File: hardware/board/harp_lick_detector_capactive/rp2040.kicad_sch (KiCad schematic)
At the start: 40 parts, among them J1 USB_C_Receptacle_USB2.0, J3 Conn_01x03_Male, J4 AudioJack3, U1 RP2040, U2 W25Q128JVS, U3 ADUM4160, U4 TPD2EUSB30, X1 ECS-TXO-2016

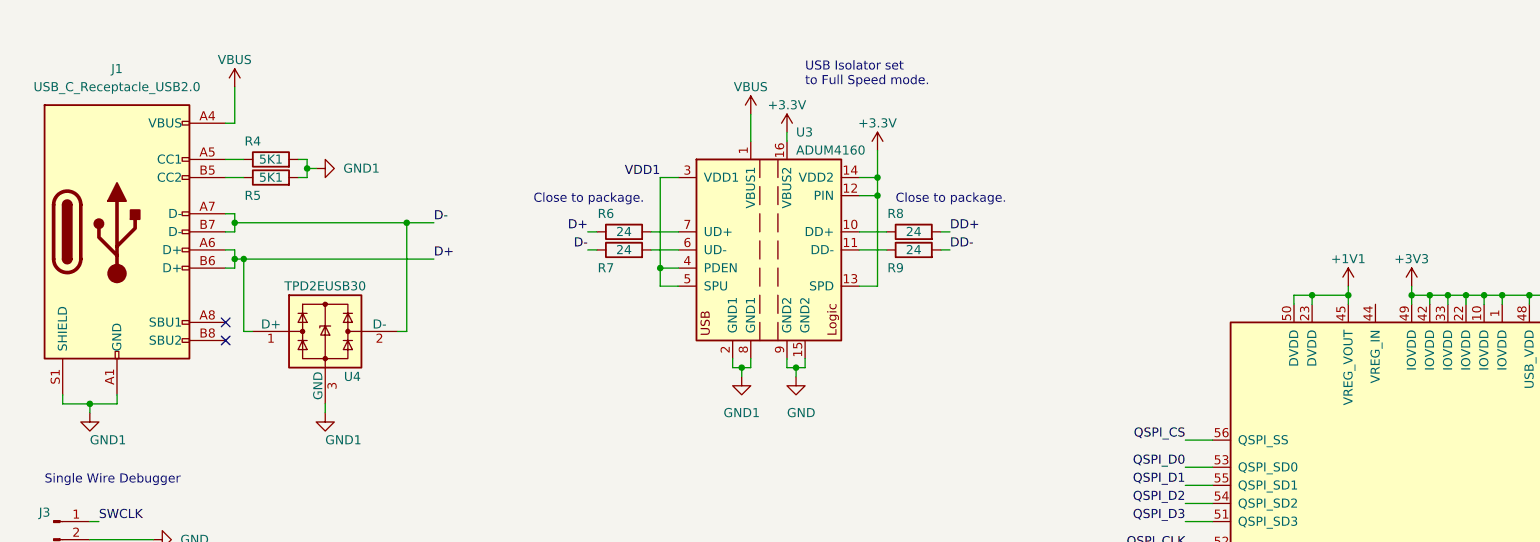
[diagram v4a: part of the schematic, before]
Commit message: pass eeschema drc
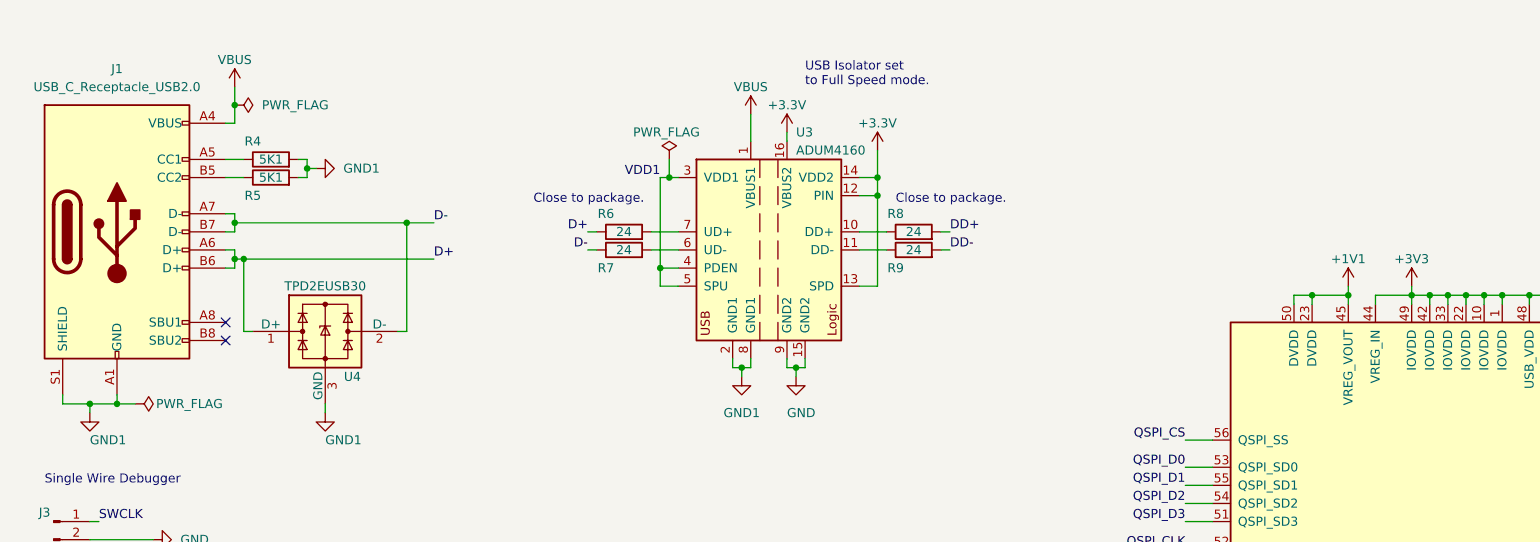
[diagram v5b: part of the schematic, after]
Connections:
- net +3V3: now also U1.44 (VREG_IN)
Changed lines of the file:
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@@
   (junction (at 44.45 44.45) (diameter 0) (color 0 0 0 0)
   )
+  (junction (at 44.45 27.94) (diameter 0) (color 0 0 0 0)
+  )
+  (junction (at 27.94 69.85) (diameter 0) (color 0 0 0 0)
+  )
   (junction (at 86.36 189.23) (diameter 0) (color 0 0 0 0)
   )
@@
   (junction (at 115.57 64.77) (diameter 0) (color 0 0 0 0)
   )
+  (junction (at 105.41 38.1) (diameter 0) (color 0 0 0 0)
+  )
   (junction (at 123.19 64.77) (diameter 0) (color 0 0 0 0)
   )
@@
   (no_connect (at 245.11 147.32))
   (no_connect (at 245.11 149.86))
-  (wire (pts (xy 44.45 25.4) (xy 44.45 30.48))
+  (wire (pts (xy 44.45 25.4) (xy 44.45 27.94))
     (stroke (width 0) (type default) (color 0 0 0 0))
   )
@@
     (stroke (width 0) (type default) (color 0 0 0 0))
   )
+  (wire (pts (xy 105.41 35.56) (xy 105.41 38.1))
+    (stroke (width 0) (type default) (color 0 0 0 0))
+  )
   (wire (pts (xy 245.11 66.04) (xy 246.38 66.04))
     (stroke (width 0) (type default) (color 0 0 0 0))
   )
+  (wire (pts (xy 209.55 54.61) (xy 204.47 54.61))
+    (stroke (width 0) (type default) (color 0 0 0 0))
+  )
   (wire (pts (xy 68.58 44.45) (xy 72.39 44.45))
     (stroke (width 0) (type default) (color 0 0 0 0))
@@
     (stroke (width 0) (type default) (color 0 0 0 0))
   )
-  (wire (pts (xy 106.68 38.1) (xy 104.14 38.1))
+  (wire (pts (xy 106.68 38.1) (xy 105.41 38.1))
     (stroke (width 0) (type default) (color 0 0 0 0))
   )
@@
     (stroke (width 0) (type default) (color 0 0 0 0))
   )
-  (wire (pts (xy 116.84 63.5) (xy 116.84 64.77))
-    (stroke (width 0) (type default) (color 0 0 0 0))
-  )
   (wire (pts (xy 254 66.04) (xy 255.27 66.04))
     (stroke (width 0) (type default) (color 0 0 0 0))
@@
     (stroke (width 0) (type default) (color 0 0 0 0))
   )
+  (wire (pts (xy 116.84 63.5) (xy 116.84 64.77))
+    (stroke (width 0) (type default) (color 0 0 0 0))
+  )
   (wire (pts (xy 120.65 179.07) (xy 120.65 180.34))
     (stroke (width 0) (type default) (color 0 0 0 0))
@@
     (stroke (width 0) (type default) (color 0 0 0 0))
   )
+  (wire (pts (xy 204.47 54.61) (xy 204.47 55.88))
+    (stroke (width 0) (type default) (color 0 0 0 0))
+  )
   (wire (pts (xy 245.11 63.5) (xy 246.38 63.5))
     (stroke (width 0) (type default) (color 0 0 0 0))
@@
     (stroke (width 0) (type default) (color 0 0 0 0))
   )
+  (wire (pts (xy 27.94 69.85) (xy 30.48 69.85))
+    (stroke (width 0) (type default) (color 0 0 0 0))
+  )
+  (wire (pts (xy 44.45 27.94) (xy 44.45 30.48))
+    (stroke (width 0) (type default) (color 0 0 0 0))
+  )
   (wire (pts (xy 245.11 137.16) (xy 255.27 137.16))
     (stroke (width 0) (type default) (color 0 0 0 0))
@@
     (stroke (width 0) (type default) (color 0 0 0 0))
   )
+  (wire (pts (xy 105.41 38.1) (xy 104.14 38.1))
+    (stroke (width 0) (type default) (color 0 0 0 0))
+  )
   (image (at 165.1 25.4) (scale 0.172608)
     (data
@@
     (pin "1")
   )
+  (symbol (lib_id "power:PWR_FLAG") (at 105.41 35.56 0) (unit 1)
+    (in_bom yes) (on_board yes)
+    (property "Reference" "#FLG0104" (id 0) (at 105.41 33.655 0)
+      (effects (font (size 1.27 1.27)) hide)
+    )
+    (property "Value" "PWR_FLAG" (id 1) (at 100.33 31.75 0)
+      (effects (font (size 1.27 1.27)) (justify left))
+    )
+    (property "Footprint" "" (id 2) (at 105.41 35.56 0)
+      (effects (font (size 1.27 1.27)) hide)
+    )
+    (property "Datasheet" "~" (id 3) (at 105.41 35.56 0)
+      (effects (font (size 1.27 1.27)) hide)
+    )
+    (pin "1")
+  )
   (symbol (lib_id "power:GND") (at 50.8 190.5 0) (unit 1)
     (in_bom yes) (on_board yes) (fields_autoplaced)
@@
     (pin "2")
   )
+  (symbol (lib_id "power:PWR_FLAG") (at 44.45 27.94 270) (unit 1)
+    (in_bom yes) (on_board yes) (fields_autoplaced)
+    (property "Reference" "#FLG0101" (id 0) (at 46.355 27.94 0)
+      (effects (font (size 1.27 1.27)) hide)
+    )
+    (property "Value" "PWR_FLAG" (id 1) (at 48.26 27.9399 90)
+      (effects (font (size 1.27 1.27)) (justify left))
+    )
+    (property "Footprint" "" (id 2) (at 44.45 27.94 0)
+      (effects (font (size 1.27 1.27)) hide)
+    )
+    (property "Datasheet" "~" (id 3) (at 44.45 27.94 0)
+      (effects (font (size 1.27 1.27)) hide)
+    )
+    (pin "1")
+  )
   (symbol (lib_id "power:GND1") (at 115.57 66.04 0) (unit 1)
     (in_bom yes) (on_board yes) (fields_autoplaced)
@@
     (pin "2")
   )
+  (symbol (lib_id "power:PWR_FLAG") (at 30.48 69.85 270) (unit 1)
+    (in_bom yes) (on_board yes)
+    (property "Reference" "#FLG0106" (id 0) (at 32.385 69.85 0)
+      (effects (font (size 1.27 1.27)) hide)
+    )
+    (property "Value" "PWR_FLAG" (id 1) (at 38.1 69.85 90))
+    (property "Footprint" "" (id 2) (at 30.48 69.85 0)
+      (effects (font (size 1.27 1.27)) hide)
+    )
+    (property "Datasheet" "~" (id 3) (at 30.48 69.85 0)
+      (effects (font (size 1.27 1.27)) hide)
+    )
+    (pin "1")
+  )
   (symbol (lib_id "Interface_USB:ADUM4160") (at 119.38 48.26 0) (unit 1)

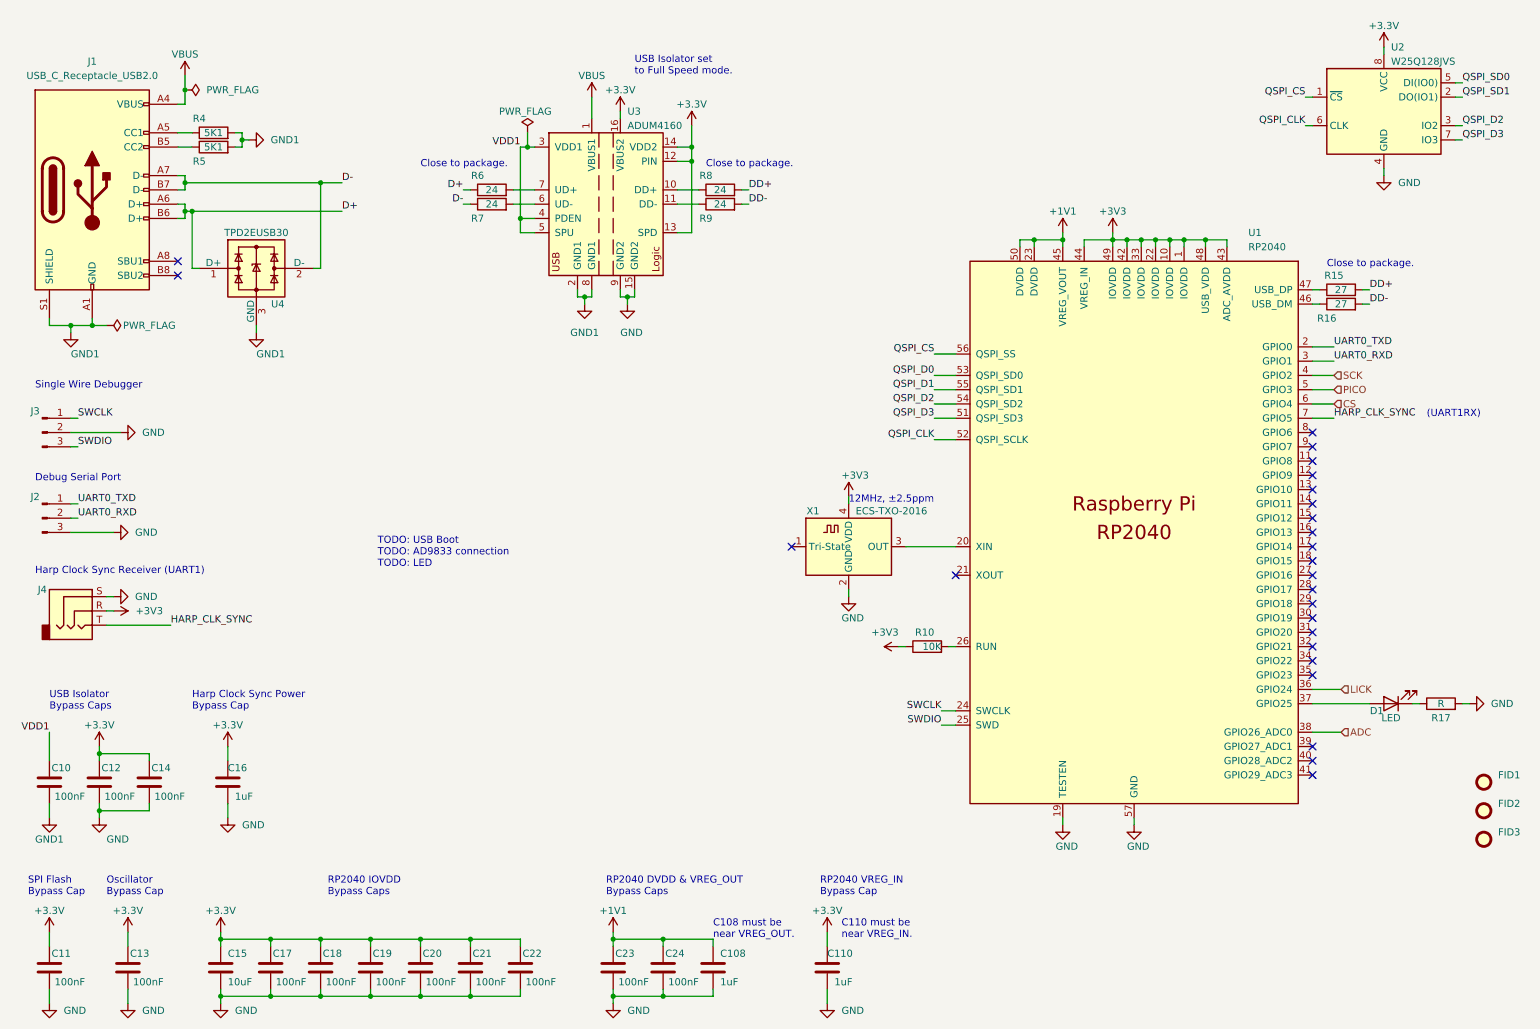
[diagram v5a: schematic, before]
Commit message: complete bom assignment
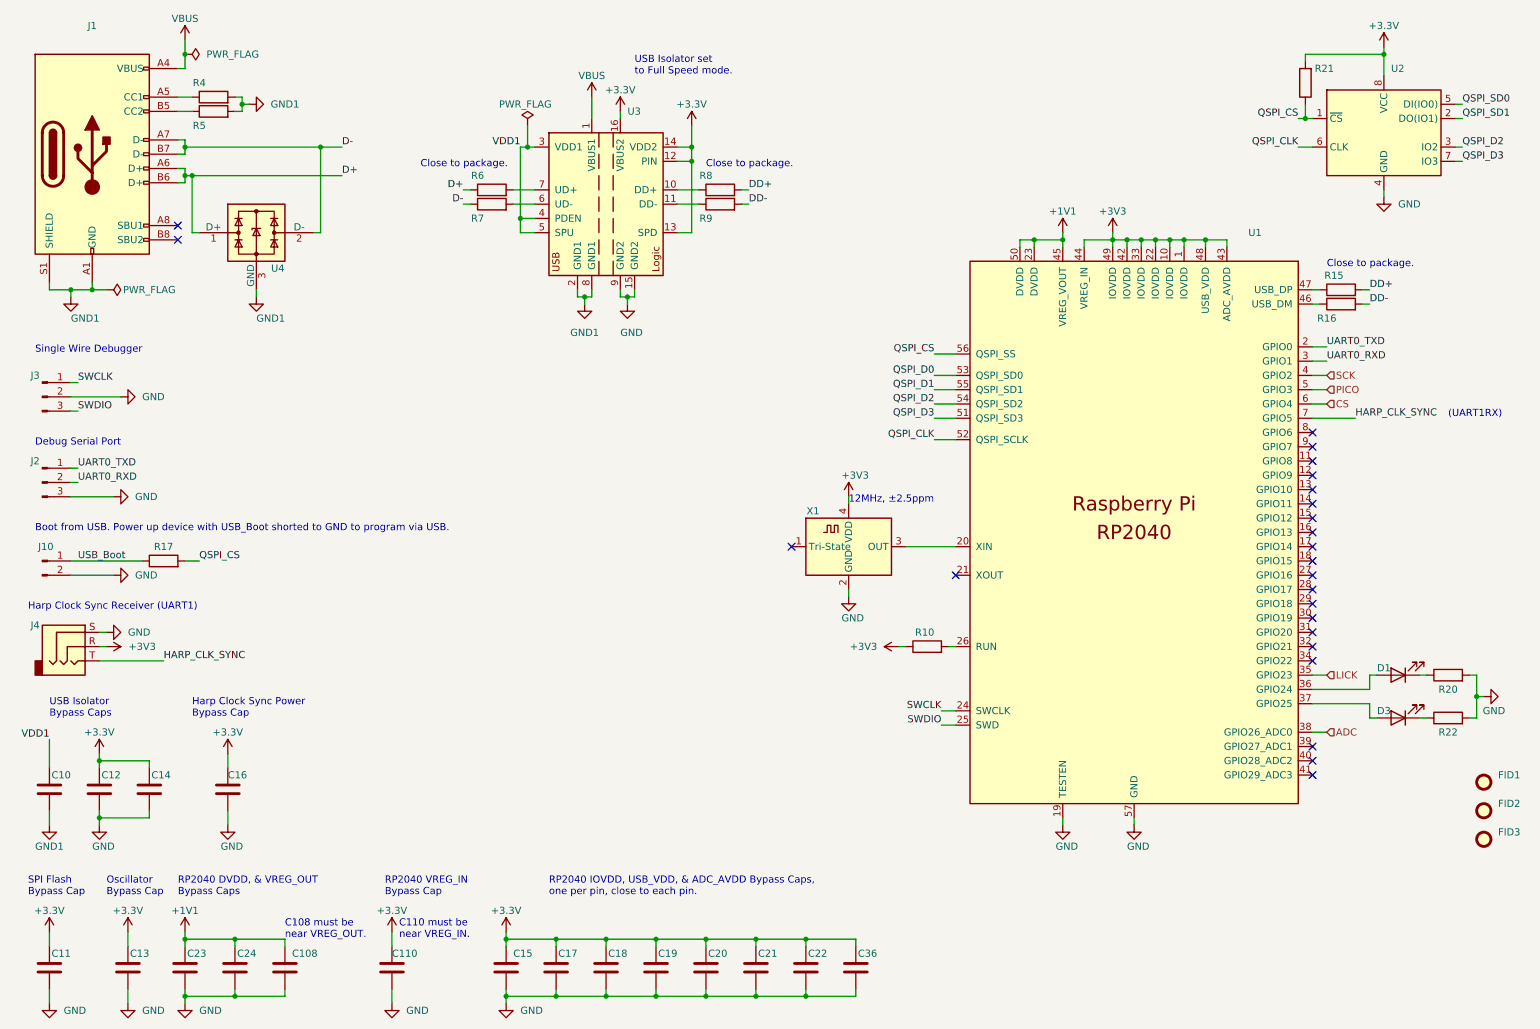
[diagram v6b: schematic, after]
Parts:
- added C36: (no value), symbol Device:C
- added D3: (no value), symbol Device:LED
- added J10: (no value), symbol Connector:Conn_01x02_Male
- added R20, R21, R22: (no value), symbol Device:R
- C10, C11, C12, C13, C14, C17, C18, C19, C20, C21, C22, C23, C24: value 100nF -> (none); footprint Capacitor_SMD:C_0603_1608Metric_Pad1.08x0.95mm_HandSolder -> (none)
- C108, C110, C16: value 1uF -> (none); footprint Capacitor_SMD:C_0603_1608Metric_Pad1.08x0.95mm_HandSolder -> (none)
- C15: value 10uF -> (none); footprint Capacitor_SMD:C_0805_2012Metric -> (none)
- D1: value LED -> (none); Link (none) -> https://www.digikey.com/en/products/detail/sunled/XZCDGK53W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; Manufacturer (none) -> SunLED; Manufacturer Number (none) -> XZCDGK53W-1VF; Notes (none) -> 2mA, 98mcd, green
- FID1: value Fiducial -> (none); footprint Fiducial:Fiducial_0.5mm_Mask1mm -> (none)
- FID2, FID3: value ~ -> (none); footprint Fiducial:Fiducial_0.5mm_Mask1mm -> (none)
- J1: value USB_C_Receptacle_USB2.0 -> (none); footprint Connector_USB:USB_C_Receptacle_Amphenol_12401610E4-2A_CircularHoles -> (none)
- J2: value ~ -> (none)
- J3: value Conn_01x03_Male -> (none)
- J4: value AudioJack3 -> (none); Link (none) -> https://www.digikey.com/en/products/detail/cui-devices/SJ-3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
- R10: value 10K -> (none); footprint Resistor_SMD:R_0402_1005Metric_Pad0.72x0.64mm_HandSolder -> (none)
- R15, R16: value 27 -> (none); footprint Resistor_SMD:R_0603_1608Metric_Pad0.98x0.95mm_HandSolder -> (none); Link https://www.digikey.com/en/products/detail/yageo/RC0603FR-0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 -> https://www.digikey.com/en/products/detail/yageo/RC0402FR-0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; Manufacturer Number RC0603FR-0727RL -> RC0402FR-0727RL; Tolerance (none) -> 1%
- R17: value R -> (none); Link (none) -> https://www.digikey.com/en/products/detail/yageo/AC0402FR-1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; Manufacturer (none) -> Yageo; Manufacturer Number (none) -> AC0402FR-131KL; Tolerance (none) -> 1%
- R4, R5: value 5K1 -> (none); footprint Resistor_SMD:R_0603_1608Metric_Pad0.98x0.95mm_HandSolder -> (none)
- R6, R7, R8, R9: value 24 -> (none); Link (none) -> https://www.digikey.com/en/products/detail/yageo/AC0402FR-0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; Manufacturer (none) -> Yageo; Manufacturer Number (none) -> AC0402FR-0724RL; Tolerance (none) -> 1%
- U1: value RP2040 -> (none); footprint RP2040_minimal:RP2040-QFN-56 -> (none)
- U2: value W25Q128JVS -> (none); footprint Package_SO:SOIC-8_5.23x5.23mm_P1.27mm -> (none)
- U3: value ADUM4160 -> (none); footprint Package_SO:SOIC-16W_7.5x10.3mm_P1.27mm -> (none)
- U4: value TPD2EUSB30 -> (none); footprint Package_TO_SOT_SMD:Texas_DRT-3 -> (none)
- X1: value ECS-TXO-2016 -> (none); footprint Crystal:Crystal_SMD_2016-4Pin_2.0x1.6mm -> (none)
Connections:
- net +3V3: now also C36.2, R21.2
- net GND: now also C36.1, J10.2 (Pin_2), R20.2, R22.2; no longer R17.2
- net LICK: now also U1.35 (GPIO23); no longer U1.36 (GPIO24)
- net QSPI_CS: now also R17.2, R21.1
- net at D1.2 (A): now also U1.36 (GPIO24); no longer U1.37 (GPIO25)
- net at D1.1 (K): now also R20.1; no longer R17.1
- new net: D3.2 (A), U1.37 (GPIO25)
- new net: D3.1 (K), R22.1
- new net USB_Boot: J10.1 (Pin_1), R17.1
- no-connect marks 25 -> 24
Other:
- note added: "Boot from USB. Power up device with USB_Boot shorted to GND to program via USB."
- note added: "RP2040 DVDD, & VREG_OUT Bypass Caps"
- note added: "RP2040 IOVDD, USB_VDD, & ADC_AVDD Bypass Caps, one per pin, close to each pin."
- note removed: "RP2040 DVDD & VREG_OUT Bypass Caps"
- note removed: "RP2040 IOVDD Bypass Caps"
- note removed: "TODO: USB Boot TODO: AD9833 connection TODO: LED"
- moved on the sheet: C10, C108, C110, C12, C14, C15, C16, C17, C18, C19, C20, C21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

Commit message: loosely place components
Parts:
- C10, C11, C12, C13, C14, C17, C18, C19, C20, C21, C22, C23, C24, C36: Link https://www.digikey.com/en/products/detail/samsung-electro-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 -> https://www.digikey.com/en/products/detail/walsin-technolog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; Manufacturer Samsung Electro-Mechanics -> Walson Technology Corporation; Manufacturer Number CL10B104KB8NNWC -> 0402B104K160CT; Rated Voltage 50V -> 16V
